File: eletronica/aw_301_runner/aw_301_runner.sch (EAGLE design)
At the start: 9 parts, among them IC1 ATTINY2313V, Q1 4 Mhz

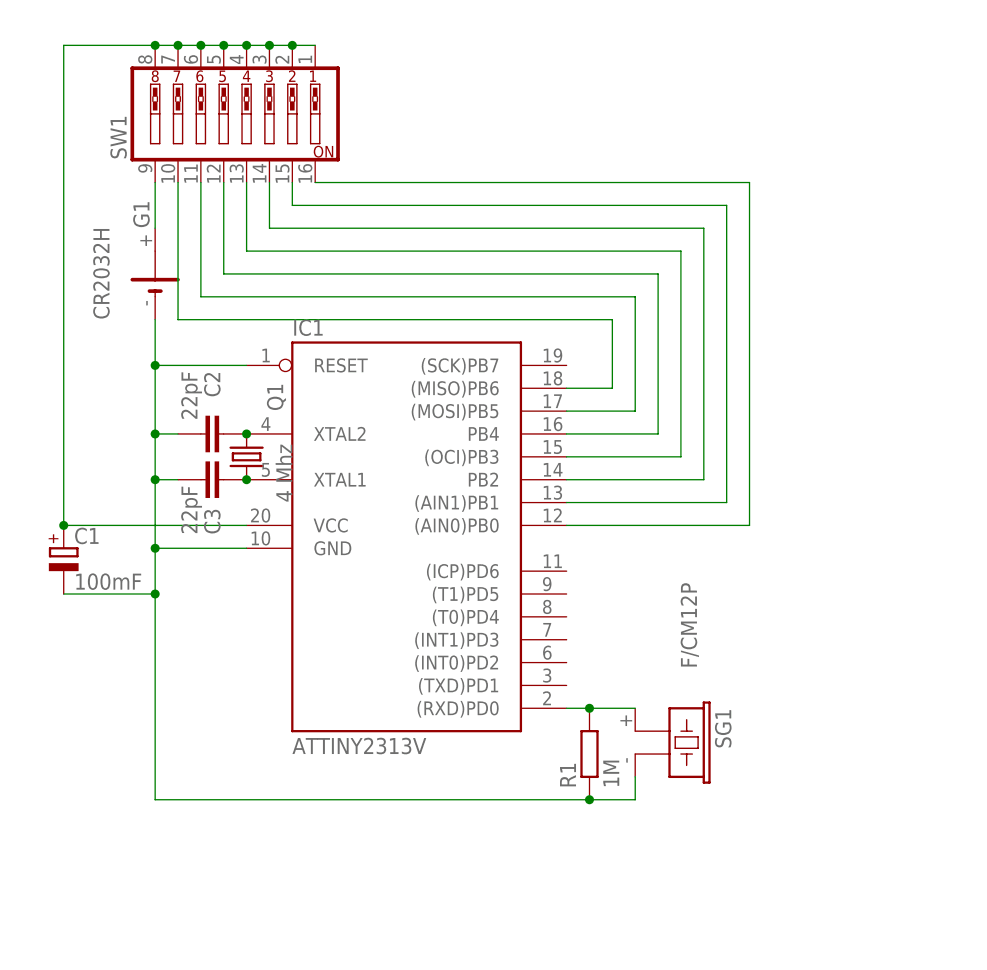
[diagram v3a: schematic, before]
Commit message: 
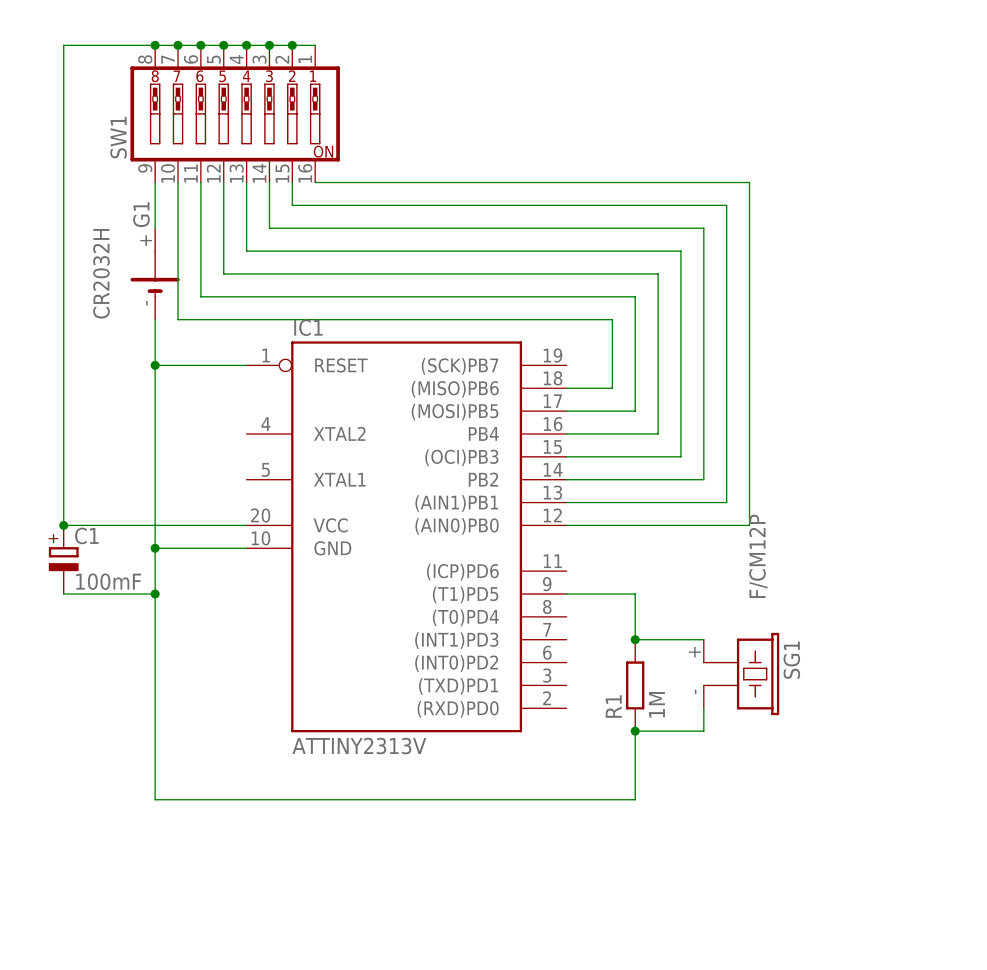
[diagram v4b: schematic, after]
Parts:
- removed C2, C3: 22pF, rcl:C-EU025-025X050
- removed Q1: 4 Mhz, crystal:CRYSTALHC49U70
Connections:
- removed net N$2: C2.2, IC1.XTAL2, Q1.2
- removed net N$3: C3.2, IC1.XTAL1, Q1.1
- removed net N$6: IC1.(RXD)PD0, R1.2, SG1.1
- new net N$4: IC1.(T1)PD5, R1.2, SG1.1
- net GND: no longer C2.1, C3.1
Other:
- moved on the sheet: R1, SG1

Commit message: 
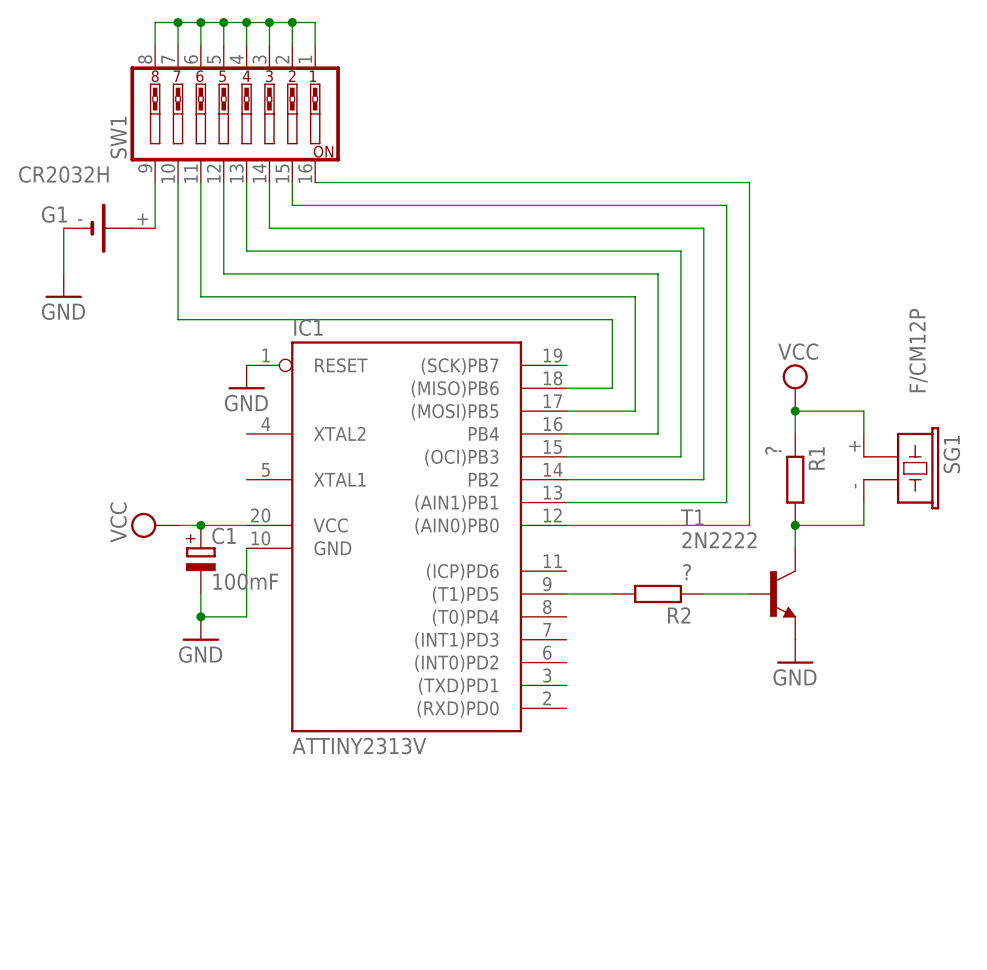
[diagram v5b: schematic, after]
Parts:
- added R2: ?, rcl:R-EU_0207/10
- added T1: 2N2222, transistor:2N2222
- R1: value 1M -> ?
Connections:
- new net N$1: SW1.1, SW1.2, SW1.3, SW1.4, SW1.5, SW1.6, SW1.7, SW1.8
- new net N$2: IC1.(T1)PD5, R2.2
- new net N$3: R2.1, T1.B
- net GND: now also T1.E; no longer R1.1, SG1.2
- net N$4: now also SG1.2, T1.C; no longer IC1.(T1)PD5, SG1.1
- net VCC: now also R1.1, SG1.1; no longer SW1.1, SW1.2, SW1.3, SW1.4, SW1.5, SW1.6, SW1.7, SW1.8
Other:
- moved on the sheet: C1, G1, R1, SG1

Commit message: 
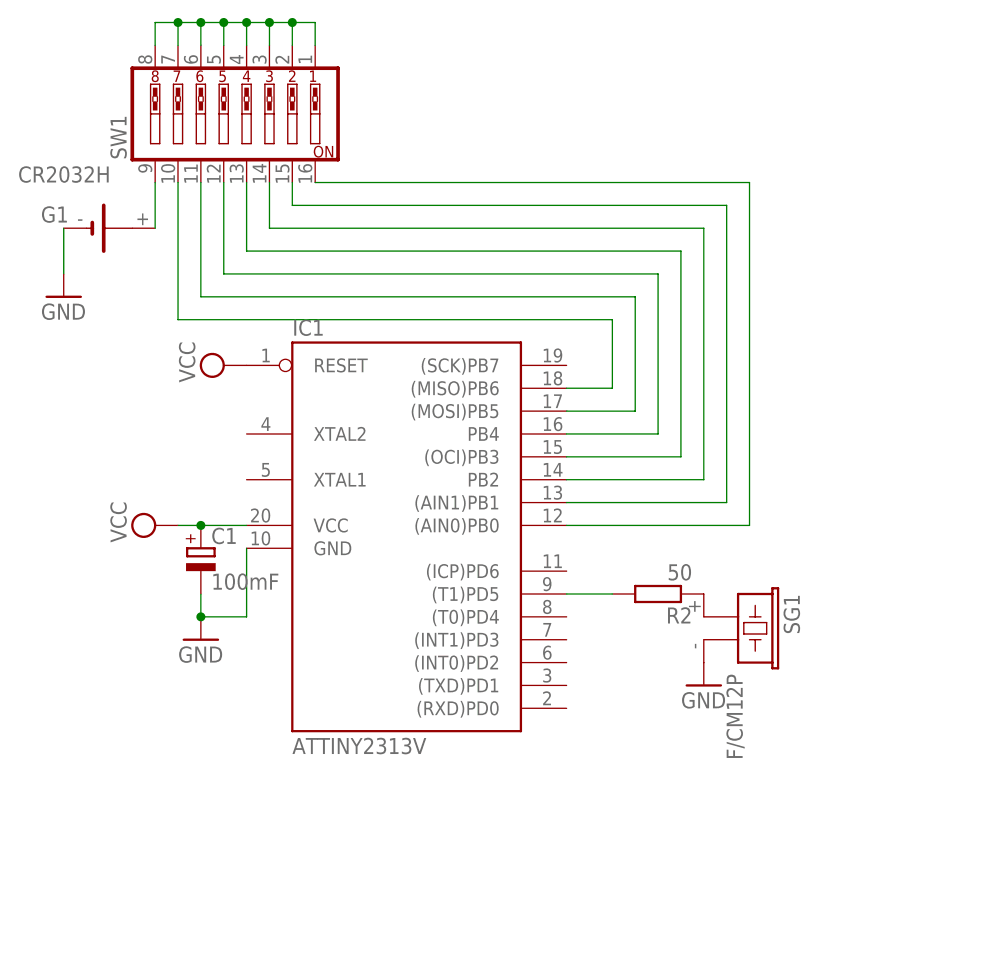
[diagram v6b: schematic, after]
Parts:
- removed R1: ?, rcl:R-EU_0207/10
- removed T1: 2N2222, transistor:2N2222
- R2: value ? -> 50
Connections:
- removed net N$1: SW1.1, SW1.2, SW1.3, SW1.4, SW1.5, SW1.6, SW1.7, SW1.8
- removed net N$4: R1.2, SG1.2, T1.C
- net GND: now also SG1.2; no longer IC1.RESET, T1.E
- net N$3: now also SG1.1; no longer T1.B
- net VCC: now also IC1.RESET, SW1.1, SW1.2, SW1.3, SW1.4, SW1.5, SW1.6, SW1.7, SW1.8; no longer R1.1, SG1.1
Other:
- moved on the sheet: SG1
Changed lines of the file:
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@@
 <part name="SW1" library="special" deviceset="SW_DIP-8" device=""/>
 <part name="G1" library="battery" deviceset="CR2032H" device=""/>
-<part name="SG1" library="buzzer" deviceset="F/CM12P" device=""/>
 <part name="C1" library="resistor" deviceset="CPOL-EU" device="E2.5-6" value="100mF"/>
-<part name="R2" library="rcl" deviceset="R-EU_" device="0207/10" value="?"/>
-<part name="T1" library="transistor" deviceset="2N2222" device=""/>
-<part name="GND1" library="supply1" deviceset="GND" device=""/>
-<part name="R1" library="rcl" deviceset="R-EU_" device="0207/10" value="?"/>
-<part name="SUPPLY1" library="supply2" deviceset="VCC" device=""/>
+<part name="R2" library="rcl" deviceset="R-EU_" device="0207/10" value="50"/>
 <part name="SUPPLY2" library="supply2" deviceset="VCC" device=""/>
 <part name="GND2" library="supply1" deviceset="GND" device=""/>
 <part name="GND3" library="supply1" deviceset="GND" device=""/>
-<part name="GND4" library="supply1" deviceset="GND" device=""/>
+<part name="SG1" library="buzzer" deviceset="F/CM12P" device=""/>
+<part name="SUPPLY1" library="supply2" deviceset="VCC" device=""/>
+<part name="GND1" library="supply1" deviceset="GND" device=""/>
 </parts>
 <sheets>
@@
 <attribute name="VALUE" x="50.8" y="71.12" size="1.778" layer="96"/>
 </instance>
-<instance part="SG1" gate="G$1" x="147.32" y="40.64" smashed="yes" rot="R270">
-<attribute name="NAME" x="153.67" y="43.18" size="1.778" layer="95" rot="R270"/>
-<attribute name="VALUE" x="149.86" y="57.15" size="1.778" layer="96" rot="R270"/>
-</instance>
 <instance part="C1" gate="G$1" x="71.12" y="30.48"/>
 <instance part="R2" gate="G$1" x="121.92" y="25.4" rot="R180"/>
-<instance part="T1" gate="G$1" x="134.62" y="25.4"/>
-<instance part="GND1" gate="1" x="137.16" y="17.78"/>
-<instance part="R1" gate="G$1" x="137.16" y="38.1" rot="R270"/>
-<instance part="SUPPLY1" gate="G$1" x="137.16" y="48.26"/>
 <instance part="SUPPLY2" gate="G$1" x="66.04" y="33.02" rot="R90"/>
 <instance part="GND2" gate="1" x="55.88" y="58.42"/>
 <instance part="GND3" gate="1" x="71.12" y="20.32"/>
-<instance part="GND4" gate="1" x="76.2" y="48.26"/>
+<instance part="SG1" gate="G$1" x="129.54" y="22.86" rot="R270"/>
+<instance part="SUPPLY1" gate="G$1" x="73.66" y="50.8" rot="R90"/>
+<instance part="GND1" gate="1" x="127" y="15.24"/>
 </instances>
 <busses>
@@
 <nets>
 <net name="VCC" class="0">
-<segment>
-<pinref part="R1" gate="G$1" pin="1"/>
-<pinref part="SUPPLY1" gate="G$1" pin="VCC"/>
-<wire x1="137.16" y1="45.72" x2="137.16" y2="43.18" width="0.1524" layer="91"/>
-<pinref part="SG1" gate="G$1" pin="1"/>
-<wire x1="144.78" y1="43.18" x2="144.78" y2="45.72" width="0.1524" layer="91"/>
-<wire x1="144.78" y1="45.72" x2="137.16" y2="45.72" width="0.1524" layer="91"/>
-<junction x="137.16" y="45.72"/>
-</segment>
 <segment>
 <pinref part="IC1" gate="G$1" pin="VCC"/>
@@
 <junction x="71.12" y="33.02"/>
 </segment>
+<segment>
+<pinref part="SW1" gate="A" pin="8"/>
+<wire x1="66.04" y1="86.36" x2="66.04" y2="88.9" width="0.1524" layer="91"/>
+<wire x1="66.04" y1="88.9" x2="68.58" y2="88.9" width="0.1524" layer="91"/>
+<pinref part="SW1" gate="A" pin="1"/>
+<wire x1="68.58" y1="88.9" x2="71.12" y2="88.9" width="0.1524" layer="91"/>
+<wire x1="71.12" y1="88.9" x2="73.66" y2="88.9" width="0.1524" layer="91"/>
+<wire x1="73.66" y1="88.9" x2="76.2" y2="88.9" width="0.1524" layer="91"/>
+<wire x1="76.2" y1="88.9" x2="78.74" y2="88.9" width="0.1524" layer="91"/>
+<wire x1="78.74" y1="88.9" x2="81.28" y2="88.9" width="0.1524" layer="91"/>
+<wire x1="83.82" y1="86.36" x2="83.82" y2="88.9" width="0.1524" layer="91"/>
+<wire x1="83.82" y1="88.9" x2="81.28" y2="88.9" width="0.1524" layer="91"/>
+<pinref part="SW1" gate="A" pin="2"/>
+<wire x1="81.28" y1="88.9" x2="81.28" y2="86.36" width="0.1524" layer="91"/>
+<junction x="81.28" y="88.9"/>
+<pinref part="SW1" gate="A" pin="3"/>
+<wire x1="78.74" y1="88.9" x2="78.74" y2="86.36" width="0.1524" layer="91"/>
+<junction x="78.74" y="88.9"/>
+<pinref part="SW1" gate="A" pin="4"/>
+<wire x1="76.2" y1="88.9" x2="76.2" y2="86.36" width="0.1524" layer="91"/>
+<junction x="76.2" y="88.9"/>
+<pinref part="SW1" gate="A" pin="5"/>
+<wire x1="73.66" y1="88.9" x2="73.66" y2="86.36" width="0.1524" layer="91"/>
+<junction x="73.66" y="88.9"/>
+<pinref part="SW1" gate="A" pin="6"/>
+<wire x1="71.12" y1="88.9" x2="71.12" y2="86.36" width="0.1524" layer="91"/>
+<junction x="71.12" y="88.9"/>
+<pinref part="SW1" gate="A" pin="7"/>
+<wire x1="68.58" y1="88.9" x2="68.58" y2="86.36" width="0.1524" layer="91"/>
+<junction x="68.58" y="88.9"/>
+</segment>
+<segment>
+<pinref part="IC1" gate="G$1" pin="RESET"/>
+<pinref part="SUPPLY1" gate="G$1" pin="VCC"/>
+</segment>
 </net>
 <net name="GND" class="0">
-<segment>
-<pinref part="T1" gate="G$1" pin="E"/>
-<pinref part="GND1" gate="1" pin="GND"/>
-</segment>
 <segment>
 <pinref part="G1" gate="1" pin="-"/>
@@
 </segment>
 <segment>
-<pinref part="IC1" gate="G$1" pin="RESET"/>
-<pinref part="GND4" gate="1" pin="GND"/>
+<pinref part="SG1" gate="G$1" pin="2"/>
+<pinref part="GND1" gate="1" pin="GND"/>
 </segment>
 </net>
@@
 </segment>
 </net>
-<net name="N$3" class="0">
-<segment>
-<pinref part="R2" gate="G$1" pin="1"/>
-<pinref part="T1" gate="G$1" pin="B"/>
-<wire x1="127" y1="25.4" x2="132.08" y2="25.4" width="0.1524" layer="91"/>
-</segment>
-</net>
-<net name="N$4" class="0">
-<segment>
-<pinref part="T1" gate="G$1" pin="C"/>
-<pinref part="R1" gate="G$1" pin="2"/>
-<wire x1="137.16" y1="33.02" x2="137.16" y2="30.48" width="0.1524" layer="91"/>
-<pinref part="SG1" gate="G$1" pin="2"/>
-<wire x1="144.78" y1="35.56" x2="144.78" y2="33.02" width="0.1524" layer="91"/>
-<wire x1="144.78" y1="33.02" x2="137.16" y2="33.02" width="0.1524" layer="91"/>
-<junction x="137.16" y="33.02"/>
-</segment>
-</net>
-<net name="N$1" class="0">
-<segment>
-<pinref part="SW1" gate="A" pin="8"/>
-<wire x1="66.04" y1="86.36" x2="66.04" y2="88.9" width="0.1524" layer="91"/>
-<wire x1="66.04" y1="88.9" x2="68.58" y2="88.9" width="0.1524" layer="91"/>
-<pinref part="SW1" gate="A" pin="1"/>
-<wire x1="68.58" y1="88.9" x2="71.12" y2="88.9" width="0.1524" layer="91"/>
-<wire x1="71.12" y1="88.9" x2="73.66" y2="88.9" width="0.1524" layer="91"/>
-<wire x1="73.66" y1="88.9" x2="76.2" y2="88.9" width="0.1524" layer="91"/>
-<wire x1="76.2" y1="88.9" x2="78.74" y2="88.9" width="0.1524" layer="91"/>
-<wire x1="78.74" y1="88.9" x2="81.28" y2="88.9" width="0.1524" layer="91"/>
-<wire x1="83.82" y1="86.36" x2="83.82" y2="88.9" width="0.1524" layer="91"/>
-<wire x1="83.82" y1="88.9" x2="81.28" y2="88.9" width="0.1524" layer="91"/>
-<pinref part="SW1" gate="A" pin="2"/>
-<wire x1="81.28" y1="88.9" x2="81.28" y2="86.36" width="0.1524" layer="91"/>
-<junction x="81.28" y="88.9"/>
-<pinref part="SW1" gate="A" pin="3"/>
-<wire x1="78.74" y1="88.9" x2="78.74" y2="86.36" width="0.1524" layer="91"/>
-<junction x="78.74" y="88.9"/>
-<pinref part="SW1" gate="A" pin="4"/>
-<wire x1="76.2" y1="88.9" x2="76.2" y2="86.36" width="0.1524" layer="91"/>
-<junction x="76.2" y="88.9"/>
-<pinref part="SW1" gate="A" pin="5"/>
-<wire x1="73.66" y1="88.9" x2="73.66" y2="86.36" width="0.1524" layer="91"/>
-<junction x="73.66" y="88.9"/>
-<pinref part="SW1" gate="A" pin="6"/>
-<wire x1="71.12" y1="88.9" x2="71.12" y2="86.36" width="0.1524" layer="91"/>
-<junction x="71.12" y="88.9"/>
-<pinref part="SW1" gate="A" pin="7"/>
-<wire x1="68.58" y1="88.9" x2="68.58" y2="86.36" width="0.1524" layer="91"/>
-<junction x="68.58" y="88.9"/>
-</segment>
-</net>
 <net name="N$5" class="0">
 <segment>
@@
 </segment>
 </net>
+<net name="N$3" class="0">
+<segment>
+<pinref part="R2" gate="G$1" pin="1"/>
+<pinref part="SG1" gate="G$1" pin="1"/>
+</segment>
+</net>

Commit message: 
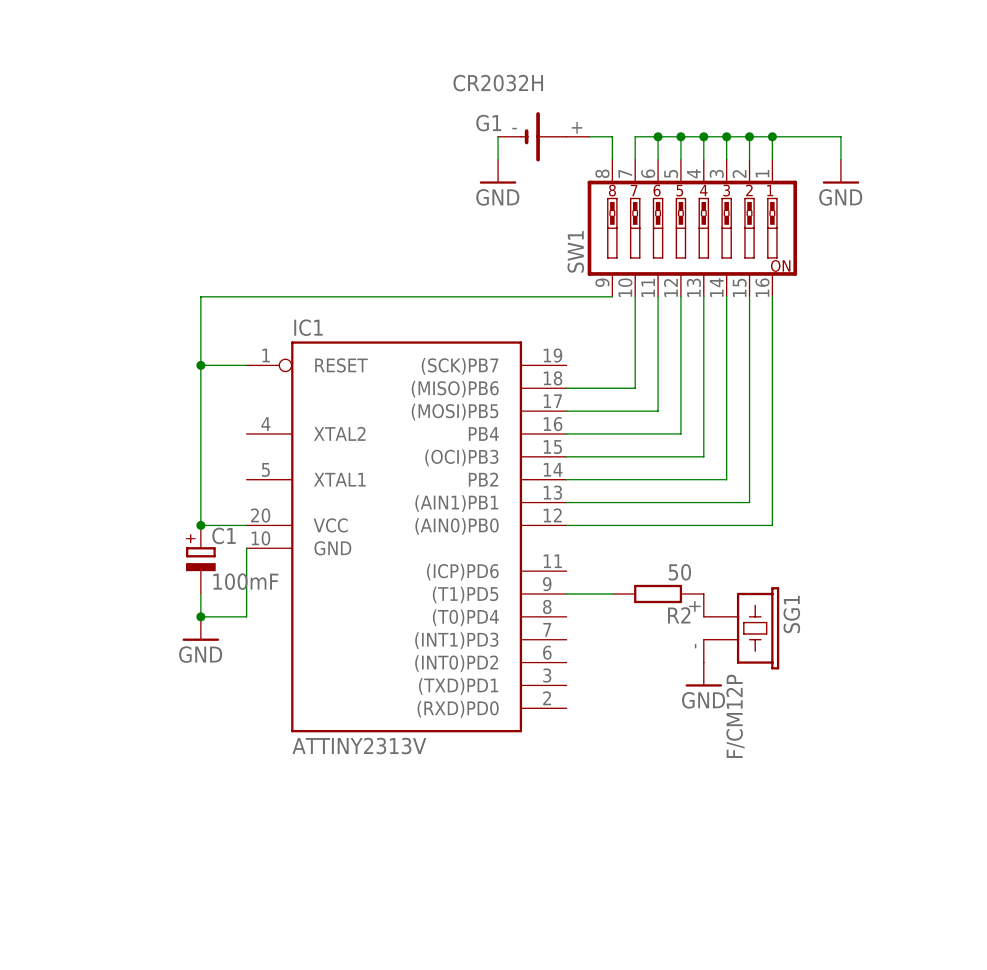
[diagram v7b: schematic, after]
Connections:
- net GND: now also SW1.1, SW1.2, SW1.3, SW1.4, SW1.5, SW1.6, SW1.7
- net N$5: now also C1.+, IC1.RESET, IC1.VCC; no longer G1.+
- net VCC: now also G1.+; no longer C1.+, IC1.RESET, IC1.VCC, SW1.1, SW1.2, SW1.3, SW1.4, SW1.5, SW1.6, SW1.7
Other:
- moved on the sheet: G1, SW1

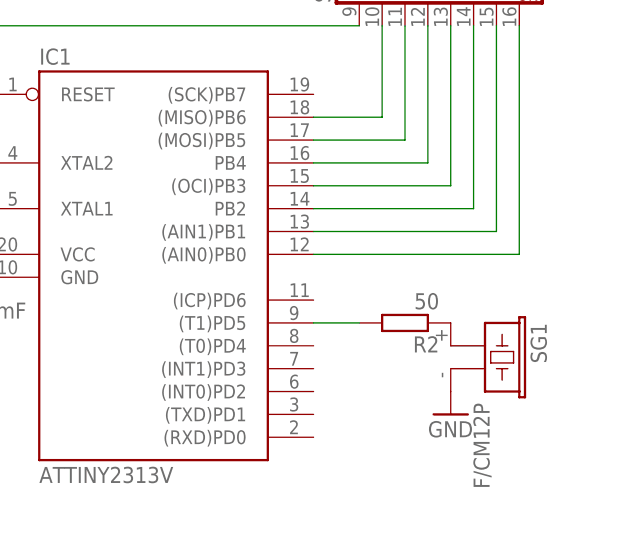
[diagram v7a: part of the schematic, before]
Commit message: 
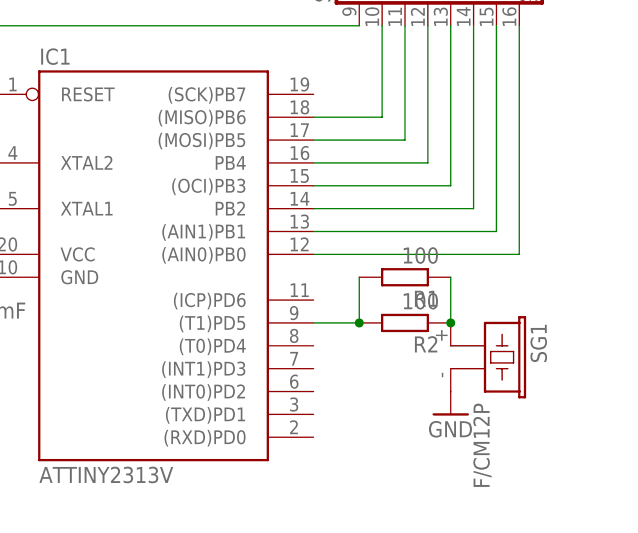
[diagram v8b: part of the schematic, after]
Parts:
- added R1: 100, rcl:R-EU_0207/10
- R2: value 50 -> 100
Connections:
- net N$2: now also R1.2
- net N$3: now also R1.1
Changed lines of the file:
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@@
 <part name="G1" library="battery" deviceset="CR2032H" device=""/>
 <part name="C1" library="resistor" deviceset="CPOL-EU" device="E2.5-6" value="100mF"/>
-<part name="R2" library="rcl" deviceset="R-EU_" device="0207/10" value="50"/>
+<part name="R2" library="rcl" deviceset="R-EU_" device="0207/10" value="100"/>
 <part name="GND2" library="supply1" deviceset="GND" device=""/>
 <part name="GND3" library="supply1" deviceset="GND" device=""/>
@@
 <part name="GND1" library="supply1" deviceset="GND" device=""/>
 <part name="GND4" library="supply1" deviceset="GND" device=""/>
+<part name="R1" library="rcl" deviceset="R-EU_" device="0207/10" value="100"/>
 </parts>
 <sheets>
@@
 <instance part="GND1" gate="1" x="127" y="15.24"/>
 <instance part="GND4" gate="1" x="142.24" y="71.12"/>
+<instance part="R1" gate="G$1" x="121.92" y="30.48" rot="R180"/>
 </instances>
 <busses>
@@
 <pinref part="R2" gate="G$1" pin="2"/>
 <wire x1="116.84" y1="25.4" x2="111.76" y2="25.4" width="0.1524" layer="91"/>
+<pinref part="R1" gate="G$1" pin="2"/>
+<wire x1="116.84" y1="25.4" x2="116.84" y2="30.48" width="0.1524" layer="91"/>
+<junction x="116.84" y="25.4"/>
 </segment>
 </net>
@@
 <pinref part="R2" gate="G$1" pin="1"/>
 <pinref part="SG1" gate="G$1" pin="1"/>
+<pinref part="R1" gate="G$1" pin="1"/>
+<wire x1="127" y1="30.48" x2="127" y2="25.4" width="0.1524" layer="91"/>
+<junction x="127" y="25.4"/>
 </segment>
 </net>
